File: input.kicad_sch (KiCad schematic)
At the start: 11 parts, among them J1 Conn_01x08

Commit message: tarjeta para raspberri, pdfs y relacion de pines
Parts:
- OPT1, OPT2, OPT3, OPT4: footprint Package_DIP:SMDIP-4_W9.53mm -> Package_DIP:DIP-4_W7.62mm
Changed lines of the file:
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@@
 			)
 		)
-		(property "Footprint" "Package_DIP:SMDIP-4_W9.53mm"
+		(property "Footprint" "Package_DIP:DIP-4_W7.62mm"
 			(at 110.49 135.89 0)
 			(effects
@@
 			)
 		)
-		(property "Footprint" "Package_DIP:SMDIP-4_W9.53mm"
+		(property "Footprint" "Package_DIP:DIP-4_W7.62mm"
 			(at 110.49 104.14 0)
 			(effects
@@
 			)
 		)
-		(property "Footprint" "Package_DIP:SMDIP-4_W9.53mm"
+		(property "Footprint" "Package_DIP:DIP-4_W7.62mm"
 			(at 110.49 120.65 0)
 			(effects
@@
 			)
 		)
-		(property "Footprint" "Package_DIP:SMDIP-4_W9.53mm"
+		(property "Footprint" "Package_DIP:DIP-4_W7.62mm"
 			(at 110.49 88.9 0)
 			(effects

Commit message: 0
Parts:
- renumbered IN2 to IN1, IN4 to IN2, IN1 to IN3, IN3 to IN4
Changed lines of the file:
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@@
 		(pin "1"
+		)
+		(instances
+			(project "electronica"
+				(path "/a1c80da3-9403-4ec6-a34a-1db23a22b009/5b7b1883-0956-4642-a84a-0fce661aecfc"
+					(reference "OPT4")
+					(unit 1)
+				)
+			)
 		)
 	)
@@
 		(pin "1"
 		)
+		(instances
+			(project "electronica"
+				(path "/a1c80da3-9403-4ec6-a34a-1db23a22b009/5b7b1883-0956-4642-a84a-0fce661aecfc"
+					(reference "J1")
+					(unit 1)
+				)
+			)
+		)
 	)
 	(symbol
@@
 		(pin "8"
 		)
+		(instances
+			(project "electronica"
+				(path "/a1c80da3-9403-4ec6-a34a-1db23a22b009/5b7b1883-0956-4642-a84a-0fce661aecfc"
+					(reference "RN2")
+					(unit 1)
+				)
+			)
+		)
 	)
 	(symbol
@@
 		(pin "1"
 		)
+		(instances
+			(project "electronica"
+				(path "/a1c80da3-9403-4ec6-a34a-1db23a22b009/5b7b1883-0956-4642-a84a-0fce661aecfc"
+					(reference "OPT2")
+					(unit 1)
+				)
+			)
+		)
 	)
 	(symbol
@@
 		(pin "1"
 		)
+		(instances
+			(project "electronica"
+				(path "/a1c80da3-9403-4ec6-a34a-1db23a22b009/5b7b1883-0956-4642-a84a-0fce661aecfc"
+					(reference "OPT3")
+					(unit 1)
+				)
+			)
+		)
 	)
 	(symbol
@@
 		(dnp no)
 		(fields_autoplaced yes)
-		(property "Reference" "IN4"
+		(property "Reference" "IN2"
 			(at 171.1325 106.68 0)
 			(effects
@@
 		(pin "1"
 		)
+		(instances
+			(project "electronica"
+				(path "/a1c80da3-9403-4ec6-a34a-1db23a22b009/5b7b1883-0956-4642-a84a-0fce661aecfc"
+					(reference "IN2")
+					(unit 1)
+				)
+			)
+		)
 	)
 	(symbol
@@
 		(dnp no)
 		(fields_autoplaced yes)
-		(property "Reference" "IN1"
+		(property "Reference" "IN3"
 			(at 181.2925 99.06 0)
 			(effects
@@
 		(pin "1"
 		)
+		(instances
+			(project "electronica"
+				(path "/a1c80da3-9403-4ec6-a34a-1db23a22b009/5b7b1883-0956-4642-a84a-0fce661aecfc"
+					(reference "IN3")
+					(unit 1)
+				)
+			)
+		)
 	)
 	(symbol
@@
 		(dnp no)
 		(fields_autoplaced yes)
-		(property "Reference" "IN3"
+		(property "Reference" "IN4"
 			(at 182.5625 104.14 0)
 			(effects
@@
 		(pin "1"
 		)
+		(instances
+			(project "electronica"
+				(path "/a1c80da3-9403-4ec6-a34a-1db23a22b009/5b7b1883-0956-4642-a84a-0fce661aecfc"
+					(reference "IN4")
+					(unit 1)
+				)
+			)
+		)
 	)
 	(symbol
@@
 		(dnp no)
 		(fields_autoplaced yes)
-		(property "Reference" "IN2"
+		(property "Reference" "IN1"
 			(at 171.1325 101.6 0)
 			(effects
@@
 		(pin "1"
 		)
+		(instances
+			(project "electronica"
+				(path "/a1c80da3-9403-4ec6-a34a-1db23a22b009/5b7b1883-0956-4642-a84a-0fce661aecfc"
+					(reference "IN1")
+					(unit 1)
+				)
+			)
+		)
 	)
 	(symbol
@@
 		(pin "1"
 		)
+		(instances
+			(project "electronica"
+				(path "/a1c80da3-9403-4ec6-a34a-1db23a22b009/5b7b1883-0956-4642-a84a-0fce661aecfc"
+					(reference "OPT1")
+					(unit 1)
+				)
+			)
+		)
 	)
 	(symbol
@@
 		(pin "8"
 		)
-	)
+		(instances
+			(project "electronica"
+				(path "/a1c80da3-9403-4ec6-a34a-1db23a22b009/5b7b1883-0956-4642-a84a-0fce661aecfc"
+					(reference "RN1")
+					(unit 1)
+				)
+			)
+		)
+	)

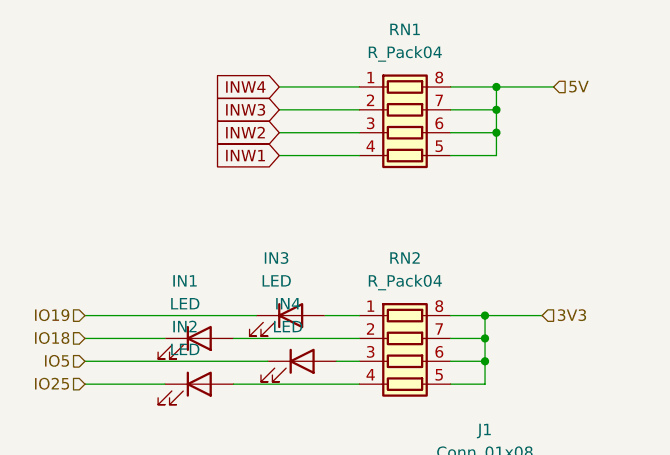
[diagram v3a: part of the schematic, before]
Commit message: en proceso de hacer el diseño, coloque el modulo de adc a i2c por que es mas barato que comprar las piezas
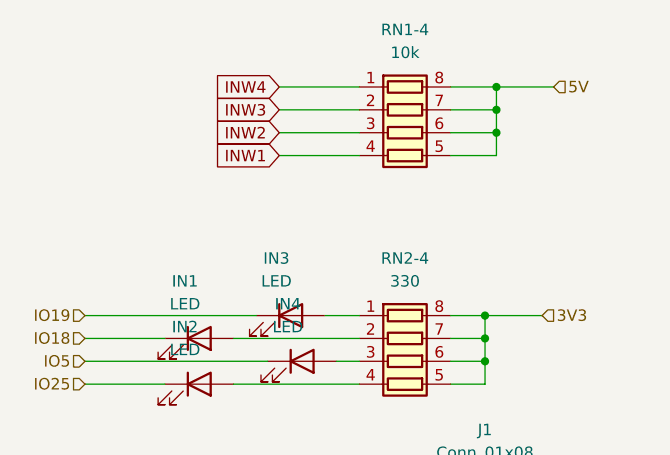
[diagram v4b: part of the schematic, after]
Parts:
- RN1-4: renamed from RN1; value R_Pack04 -> 10k
- RN2-4: renamed from RN2; value R_Pack04 -> 330
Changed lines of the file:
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@@
 		(dnp no)
 		(fields_autoplaced yes)
-		(property "Reference" "RN2"
+		(property "Reference" "RN2-4"
 			(at 195.58 99.06 90)
 			(effects
@@
 			)
 		)
-		(property "Value" "R_Pack04"
+		(property "Value" "330"
 			(at 195.58 101.6 90)
 			(effects
@@
 			(project "electronica"
 				(path "/a1c80da3-9403-4ec6-a34a-1db23a22b009/5b7b1883-0956-4642-a84a-0fce661aecfc"
-					(reference "RN2")
+					(reference "RN2-4")
 					(unit 1)
 				)
@@
 		(dnp no)
 		(fields_autoplaced yes)
-		(property "Reference" "RN1"
+		(property "Reference" "RN1-4"
 			(at 195.58 73.66 90)
 			(effects
@@
 			)
 		)
-		(property "Value" "R_Pack04"
+		(property "Value" "10k"
 			(at 195.58 76.2 90)
 			(effects
@@
 			(project "electronica"
 				(path "/a1c80da3-9403-4ec6-a34a-1db23a22b009/5b7b1883-0956-4642-a84a-0fce661aecfc"
-					(reference "RN1")
-					(unit 1)
-				)
+					(reference "RN1-4")
+					(unit 1)
+				)
